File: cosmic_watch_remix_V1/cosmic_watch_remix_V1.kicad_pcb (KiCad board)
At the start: 2 copper layers, 87.6 x 94.6 mm, 31 parts, among them IC1 MICROFJ-60035-TSV-TR1, IC2 LT3461AES6#TRMPBF, J1 Conn_01x05_Female, U1 ADS1115IDGS, U2 LM358

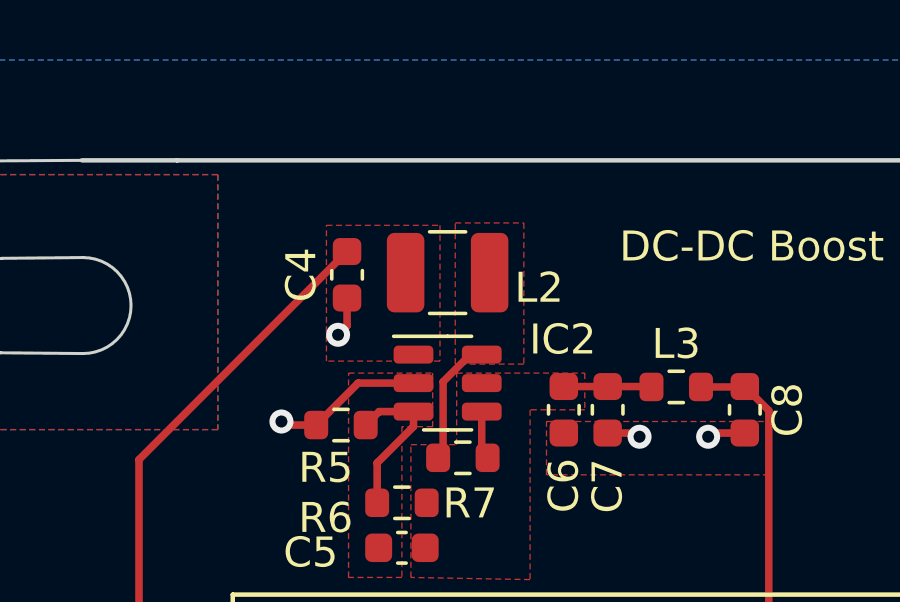
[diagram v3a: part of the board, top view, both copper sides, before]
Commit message: Fixed Inductor Power Path
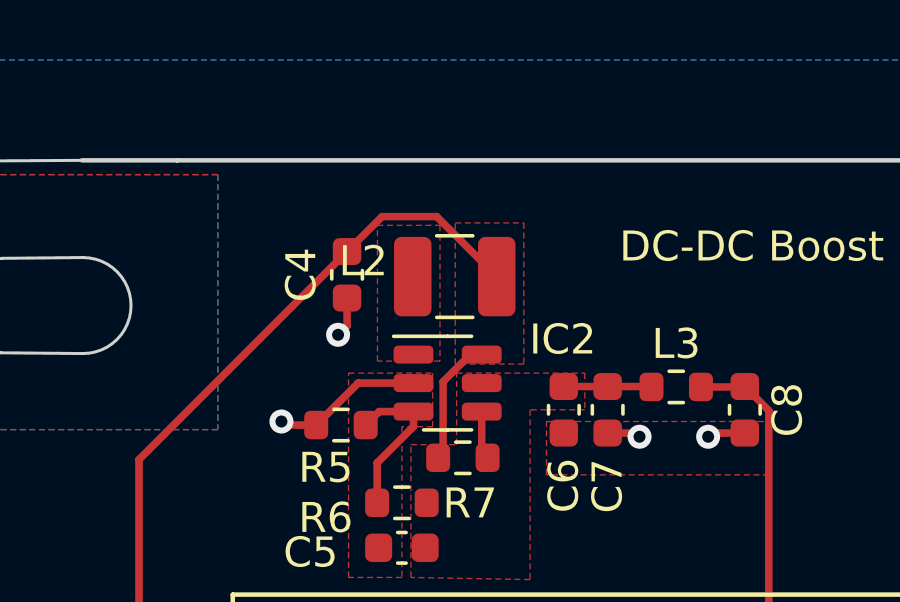
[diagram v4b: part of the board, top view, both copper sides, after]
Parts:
- C9: value ? -> 22nF
- R10: value ? -> 100k
- R6: value 280K -> 220K
- moved L2 0.27 mm to (38.4, 50.4), turned to 180 degrees
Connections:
- C4 pad 1: VCC -> unconnected-(IC2-Pad6)
- IC2 pad 1: VCC -> Net-(L2-Pad2)
- IC2 pad 6: /VIN -> unconnected-(IC2-Pad6)
- L2 pad 1: VCC -> unconnected-(IC2-Pad6)
- L2 pad 2: /VIN -> Net-(L2-Pad2)
- R7 pad 1: /VIN -> Net-(L2-Pad2)
- R8 pad 2: Net-(R8-Pad2) -> unconnected-(R8-Pad2)
- U2 pad 1: Net-(D1-Pad2) -> (no net)
- U2 pad 2: Net-(D1-Pad1) -> (no net)
- U2 pad 3: Net-(R8-Pad2) -> (no net)
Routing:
- net unconnected-(IC2-Pad6): track 0.00 -> 5.85 mm
- net Net-(L2-Pad2): track 0.00 -> 3.57 mm
- net /VIN: track 3.57 -> 0.00 mm
- net unconnected-(R8-Pad2): track 0.00 -> 2.08 mm
- net Net-(R8-Pad2): track 2.08 -> 0.00 mm
- added copper zone on F.Cu, net Net-(L2-Pad2)
- added copper zone on F.Cu, net unconnected-(IC2-Pad6)
- removed copper zone on F.Cu, net /VIN
- removed copper zone on F.Cu, net VCC
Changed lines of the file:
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@@
   (net 15 "Net-(D1-Pad2)")
   (net 16 "Net-(IC1-PadC1)")
-  (net 17 "/VIN")
+  (net 17 "Net-(L2-Pad2)")
   (net 18 "Net-(IC2-Pad4)")
-  (net 19 "Net-(R8-Pad2)")
+  (net 19 "unconnected-(IC2-Pad6)")
   (net 20 "Net-(R10-Pad2)")
   (net 21 "unconnected-(U2-Pad4)")
@@
   (net 23 "unconnected-(IC1-PadC6)")
   (net 24 "unconnected-(IC1-PadD6)")
+  (net 25 "unconnected-(R8-Pad2)")
   (footprint "Resistor_SMD:R_0603_1608Metric" (layer "F.Cu")
     (at 34.6065 55.348 180)
@@
     (pad "" smd roundrect (at -0.57 0.75 90) (size 0.92 1.21) (layers "F.Paste") (roundrect_rratio 0.25))
     (pad "" smd roundrect (at 0.57 -0.75 90) (size 0.92 1.21) (layers "F.Paste") (roundrect_rratio 0.25))
-    (pad "1" smd roundrect (at -2.475 -1.905 90) (size 1.95 0.6) (layers "F.Cu" "F.Paste" "F.Mask") (roundrect_rratio 0.25)
-      (net 15 "Net-(D1-Pad2)") (pintype "output"))
-    (pad "2" smd roundrect (at -2.475 -0.635 90) (size 1.95 0.6) (layers "F.Cu" "F.Paste" "F.Mask") (roundrect_rratio 0.25)
-      (net 14 "Net-(D1-Pad1)") (pinfunction "-") (pintype "input"))
-    (pad "3" smd roundrect (at -2.475 0.635 90) (size 1.95 0.6) (layers "F.Cu" "F.Paste" "F.Mask") (roundrect_rratio 0.25)
-      (net 19 "Net-(R8-Pad2)") (pinfunction "+") (pintype "input"))
+    (pad "1" smd roundrect (at -2.475 -1.905 90) (size 1.95 0.6) (layers "F.Cu" "F.Paste" "F.Mask") (roundrect_rratio 0.25))
+    (pad "2" smd roundrect (at -2.475 -0.635 90) (size 1.95 0.6) (layers "F.Cu" "F.Paste" "F.Mask") (roundrect_rratio 0.25))
+    (pad "3" smd roundrect (at -2.475 0.635 90) (size 1.95 0.6) (layers "F.Cu" "F.Paste" "F.Mask") (roundrect_rratio 0.25))
     (pad "4" smd roundrect (at -2.475 1.905 90) (size 1.95 0.6) (layers "F.Cu" "F.Paste" "F.Mask") (roundrect_rratio 0.25)
       (net 21 "unconnected-(U2-Pad4)") (pinfunction "V-") (pintype "power_in+no_connect"))
@@
     (fp_line (start -0.8 -0.4125) (end 0.8 -0.4125) (layer "F.Fab") (width 0.1))
     (pad "1" smd roundrect (at -0.825 0) (size 0.8 0.95) (layers "F.Cu" "F.Paste" "F.Mask") (roundrect_rratio 0.25)
-      (net 17 "/VIN") (pintype "passive"))
+      (net 17 "Net-(L2-Pad2)") (pintype "passive"))
     (pad "2" smd roundrect (at 0.825 0) (size 0.8 0.95) (layers "F.Cu" "F.Paste" "F.Mask") (roundrect_rratio 0.25)
       (net 18 "Net-(IC2-Pad4)") (pintype "passive"))
@@
       (effects (font (size 1 1) (thickness 0.15)))
     )
-    (fp_text value "?" (at 0 1.43) (layer "F.Fab")
+    (fp_text value "100k" (at 0 1.43) (layer "F.Fab")
       (effects (font (size 1 1) (thickness 0.15)))
     )
@@
       (net 16 "Net-(IC1-PadC1)") (pintype "passive"))
     (pad "2" smd roundrect (at 0.825 0 90) (size 0.8 0.95) (layers "F.Cu" "F.Paste" "F.Mask") (roundrect_rratio 0.25)
-      (net 19 "Net-(R8-Pad2)") (pintype "passive"))
+      (net 25 "unconnected-(R8-Pad2)") (pintype "passive"))
     (model "${KICAD6_3DMODEL_DIR}/Resistor_SMD.3dshapes/R_0603_1608Metric.wrl"
       (offset (xyz 0 0 0))
@@
     (fp_line (start -0.8 0.4) (end -0.8 -0.4) (layer "F.Fab") (width 0.1))
     (pad "1" smd roundrect (at -0.775 0 270) (size 0.9 0.95) (layers "F.Cu" "F.Paste" "F.Mask") (roundrect_rratio 0.25)
-      (net 2 "VCC") (pintype "passive"))
+      (net 19 "unconnected-(IC2-Pad6)") (pintype "passive"))
     (pad "2" smd roundrect (at 0.775 0 270) (size 0.9 0.95) (layers "F.Cu" "F.Paste" "F.Mask") (roundrect_rratio 0.25)
       (net 1 "GND") (pintype "passive"))
@@
       (effects (font (size 1 1) (thickness 0.15)))
     )
-    (fp_text value "280K" (at 0 1.43) (layer "F.Fab")
+    (fp_text value "220K" (at 0 1.43) (layer "F.Fab")
       (effects (font (size 1 1) (thickness 0.15)))
     )
@@
     (fp_line (start 0.8 1.45) (end -0.8 1.45) (layer "F.Fab") (width 0.1))
     (pad "1" smd roundrect (at -1.1375 -0.95) (size 1.325 0.6) (layers "F.Cu" "F.Paste" "F.Mask") (roundrect_rratio 0.25)
-      (net 2 "VCC") (pinfunction "SW") (pintype "passive"))
+      (net 17 "Net-(L2-Pad2)") (pinfunction "SW") (pintype "passive"))
     (pad "2" smd roundrect (at -1.1375 0) (size 1.325 0.6) (layers "F.Cu" "F.Paste" "F.Mask") (roundrect_rratio 0.25)
       (net 1 "GND") (pinfunction "GND") (pintype "passive"))
@@
       (net 10 "/VOUT") (pinfunction "VOUT") (pintype "passive"))
     (pad "6" smd roundrect (at 1.1375 -0.95) (size 1.325 0.6) (layers "F.Cu" "F.Paste" "F.Mask") (roundrect_rratio 0.25)
-      (net 17 "/VIN") (pinfunction "VIN") (pintype "passive"))
+      (net 19 "unconnected-(IC2-Pad6)") (pinfunction "VIN") (pintype "passive"))
     (model "${KICAD6_3DMODEL_DIR}/Package_TO_SOT_SMD.3dshapes/TSOT-23-6.wrl"
       (offset (xyz 0 0 0))
@@
       (effects (font (size 1 1) (thickness 0.15)))
     )
-    (fp_text value "?" (at 0 1.43) (layer "F.Fab")
+    (fp_text value "22nF" (at 0 1.43) (layer "F.Fab")
       (effects (font (size 1 1) (thickness 0.15)))
     )
@@
   )
   (footprint "Inductor_SMD:L_1210_3225Metric" (layer "F.Cu")
-    (at 38.1625 50.268)
+    (at 38.4 50.4 180)
     (descr "Inductor SMD 1210 (3225 Metric), square (rectangular) end terminal, IPC_7351 nominal, (Body size source: http://www.tortai-tech.com/upload/download/2011102023233369053.pdf), generated with kicad-footprint-generator")
     (tags "inductor")
@@
     (fp_line (start 1.6 1.25) (end -1.6 1.25) (layer "F.Fab") (width 0.1))
     (fp_line (start -1.6 1.25) (end -1.6 -1.25) (layer "F.Fab") (width 0.1))
-    (pad "1" smd roundrect (at -1.4 0) (size 1.25 2.65) (layers "F.Cu" "F.Paste" "F.Mask") (roundrect_rratio 0.2)
-      (net 2 "VCC") (pinfunction "1") (pintype "passive"))
-    (pad "2" smd roundrect (at 1.4 0) (size 1.25 2.65) (layers "F.Cu" "F.Paste" "F.Mask") (roundrect_rratio 0.2)
-      (net 17 "/VIN") (pinfunction "2") (pintype "passive"))
+    (pad "1" smd roundrect (at -1.4 0 180) (size 1.25 2.65) (layers "F.Cu" "F.Paste" "F.Mask") (roundrect_rratio 0.2)
+      (net 19 "unconnected-(IC2-Pad6)") (pinfunction "1") (pintype "passive"))
+    (pad "2" smd roundrect (at 1.4 0 180) (size 1.25 2.65) (layers "F.Cu" "F.Paste" "F.Mask") (roundrect_rratio 0.2)
+      (net 17 "Net-(L2-Pad2)") (pinfunction "2") (pintype "passive"))
     (model "${KICAD6_3DMODEL_DIR}/Inductor_SMD.3dshapes/L_1210_3225Metric.wrl"
       (offset (xyz 0 0 0))
@@
   (segment (start 38.01202 56.19748) (end 38.01202 53.904408) (width 0.25) (layer "F.Cu") (net 17))
   (segment (start 39.3 54.9) (end 39.3 56.1685) (width 0.25) (layer "F.Cu") (net 18))
-  (segment (start 27.635 111.475) (end 27.635 113.55) (width 0.254) (layer "F.Cu") (net 19))
+  (segment (start 37.8 48.4) (end 35.9755 48.4) (width 0.25) (layer "F.Cu") (net 19))
+  (segment (start 39.8 50.4) (end 37.8 48.4) (width 0.25) (layer "F.Cu") (net 19))
+  (segment (start 35.9755 48.4) (end 35.130112 49.245388) (width 0.25) (layer "F.Cu") (net 19))
   (segment (start 26.365 106.525) (end 27.635 106.525) (width 0.254) (layer "F.Cu") (net 20))
   (segment (start 28.171 98.829) (end 28.171 80.99) (width 0.254) (layer "F.Cu") (net 20))
@@
   (segment (start 26.365 105.465) (end 26.365 106.525) (width 0.254) (layer "F.Cu") (net 20))
   (segment (start 25.9 105) (end 26.365 105.465) (width 0.254) (layer "F.Cu") (net 20))
+  (segment (start 27.635 111.475) (end 27.635 113.55) (width 0.254) (layer "F.Cu") (net 25))
   (zone (net 1) (net_name "GND") (layer "F.Cu") (hatch edge 0.508)
     (connect_pads (clearance 0.254))
@@
     )
   )
-  (zone (net 17) (net_name "/VIN") (layer "F.Cu") (hatch edge 0.508)
+  (zone (net 19) (net_name "unconnected-(IC2-Pad6)") (layer "F.Cu") (hatch edge 0.508)
     (connect_pads (clearance 0.254))
     (min_thickness 0.254) (filled_areas_thickness no)
@@
     )
   )
-  (zone (net 2) (net_name "VCC") (layer "F.Cu") (hatch edge 0.508)
+  (zone (net 17) (net_name "Net-(L2-Pad2)") (layer "F.Cu") (hatch edge 0.508)
     (connect_pads (clearance 0.254))
     (min_thickness 0.25) (filled_areas_thickness no)
@@
       (pts
         (xy 37.9085 53.216)
-        (xy 34.1225 53.216)
-        (xy 34.1225 48.69)
+        (xy 35.8225 53.216)
+        (xy 35.8225 48.69)
         (xy 37.9085 48.69)
       )
